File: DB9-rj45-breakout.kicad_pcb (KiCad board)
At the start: 2 copper layers, 32 x 33 mm, 6 parts, among them CN1 1x9, CN2 1x8, SW1 spdt

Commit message: fixed switch to choose 2nd button between up and 2nd button
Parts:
- turned SW1 to 180 degrees
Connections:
- CN2 pad 2: Net-(CN2-Pad2) -> /up
- CN2 pad 7: /b -> Net-(CN2-Pad7)
- SW1 pad 1: /b -> /up
- SW1 pad 2: /up -> Net-(CN2-Pad7)
- SW1 pad 3: Net-(CN2-Pad2) -> /b
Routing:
- net Net-(CN2-Pad7): track 0.00 -> 16.1 mm
- net /b: track 25.4 -> 12.4 mm
- net Net-(CN2-Pad2): track 11.1 -> 0.00 mm
- net /up: track 10.9 -> 20.0 mm
- net /left: track 21.0 -> 20.5 mm
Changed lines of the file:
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@@
     (thickness 1.6)
     (drawings 7)
-    (tracks 43)
+    (tracks 47)
     (zones 0)
     (modules 6)
@@
   (net 8 /GND)
   (net 9 /b)
-  (net 10 "Net-(CN2-Pad2)")
+  (net 10 "Net-(CN2-Pad7)")
   (net_class Default "This is the default net class."
     (clearance 0.2)
@@
     (add_net /up)
     (add_net "Net-(CN1-Pad5)")
-    (add_net "Net-(CN2-Pad2)")
+    (add_net "Net-(CN2-Pad7)")
   )
   (module connectors:DB9 (layer F.Cu)
@@
       (net 7 /5V))
     (pad 7 thru_hole circle (at -2.54 -2.54) (size 1.5 1.5) (drill 0.89) (layers *.Cu *.Mask)
-      (net 9 /b))
+      (net 10 "Net-(CN2-Pad7)"))
     (pad 6 thru_hole circle (at -1.525 -4.32) (size 1.5 1.5) (drill 0.89) (layers *.Cu *.Mask)
       (net 6 /a))
@@
       (net 3 /down))
     (pad 2 thru_hole circle (at 2.535 -4.32) (size 1.5 1.5) (drill 0.89) (layers *.Cu *.Mask)
-      (net 10 "Net-(CN2-Pad2)"))
+      (net 2 /up))
     (pad 1 thru_hole circle (at 3.55 -2.54) (size 1.5 1.5) (drill 0.89) (layers *.Cu *.Mask)
       (net 8 /GND))
@@
   )
   (module switch:100SP1T1B4M2QE (layer F.Cu)
-    (at 150 110.5)
+    (at 150 110.5 180)
     (fp_text reference SW1 (at 0 0) (layer F.Fab) hide
       (effects (font (size 0.5 0.5) (thickness 0.125)))
@@
     (fp_line (start 6.35 3.43) (end 6.35 -3.43) (layer F.Fab) (width 0.12))
     (fp_line (start -6.35 3.43) (end -6.35 -3.43) (layer F.Fab) (width 0.12))
-    (pad 1 thru_hole circle (at -4.7 0) (size 3 3) (drill 1.85) (layers *.Cu *.Mask)
+    (pad 1 thru_hole circle (at -4.7 0 180) (size 3 3) (drill 1.85) (layers *.Cu *.Mask)
+      (net 2 /up))
+    (pad 2 thru_hole circle (at 0 0 180) (size 3 3) (drill 1.85) (layers *.Cu *.Mask)
+      (net 10 "Net-(CN2-Pad7)"))
+    (pad 3 thru_hole circle (at 4.7 0 180) (size 3 3) (drill 1.85) (layers *.Cu *.Mask)
       (net 9 /b))
-    (pad 2 thru_hole circle (at 0 0) (size 3 3) (drill 1.85) (layers *.Cu *.Mask)
-      (net 2 /up))
-    (pad 3 thru_hole circle (at 4.7 0) (size 3 3) (drill 1.85) (layers *.Cu *.Mask)
-      (net 10 "Net-(CN2-Pad2)"))
     (model ${KICAD_SYMBOL_DIR}/3d/e-switch/100SPxT1B4M2xE.stp
       (offset (xyz 0 0 -24))
@@
   (gr_line (start 166 94) (end 166 122) (layer Edge.Cuts) (width 0.05))
   (gr_line (start 134 94) (end 166 94) (layer Edge.Cuts) (width 0.05))
-  (segment (start 155.54 104.96) (end 155.54 101.92) (width 0.5) (layer F.Cu) (net 2))
-  (segment (start 150 110.5) (end 155.54 104.96) (width 0.5) (layer F.Cu) (net 2))
   (segment (start 157 120.786002) (end 157 106.15) (width 0.5) (layer B.Cu) (net 3))
   (segment (start 154.126001 123.660001) (end 157 120.786002) (width 0.5) (layer B.Cu) (net 3))
@@
   (segment (start 153.619999 102.769999) (end 152.77 101.92) (width 0.5) (layer B.Cu) (net 3))
   (segment (start 151.52 122.46) (end 151.54 122.46) (width 0.5) (layer B.Cu) (net 3))
-  (segment (start 150 104.5) (end 150 101.92) (width 0.5) (layer F.Cu) (net 4))
-  (segment (start 147.5 107) (end 150 104.5) (width 0.5) (layer F.Cu) (net 4))
-  (segment (start 147.5 116.61434) (end 147.5 107) (width 0.5) (layer F.Cu) (net 4))
-  (segment (start 150.505 119.61934) (end 147.5 116.61434) (width 0.5) (layer F.Cu) (net 4))
-  (segment (start 150.505 120.68) (end 150.505 119.61934) (width 0.5) (layer F.Cu) (net 4))
   (segment (start 147.23 101.92) (end 147.23 104.27) (width 0.5) (layer B.Cu) (net 5))
   (segment (start 143.349999 108.150001) (end 143.349999 121.349999) (width 0.5) (layer B.Cu) (net 5))
@@
   (segment (start 146.445 120.68) (end 147.5 119.625) (width 0.5) (layer B.Cu) (net 7))
   (segment (start 145.845 109.955) (end 145.3 110.5) (width 0.5) (layer F.Cu) (net 9))
-  (segment (start 145.845 99.08) (end 145.845 109.955) (width 0.5) (layer F.Cu) (net 9))
-  (segment (start 146.39934 122.46) (end 147.46 122.46) (width 0.5) (layer B.Cu) (net 9))
-  (segment (start 145 121.06066) (end 146.39934 122.46) (width 0.5) (layer B.Cu) (net 9))
-  (segment (start 145 112.92132) (end 145 121.06066) (width 0.5) (layer B.Cu) (net 9))
-  (segment (start 145.3 112.62132) (end 145 112.92132) (width 0.5) (layer B.Cu) (net 9))
-  (segment (start 145.3 110.5) (end 145.3 112.62132) (width 0.5) (layer B.Cu) (net 9))
-  (segment (start 154.7 118.515) (end 154.7 110.5) (width 0.5) (layer B.Cu) (net 10))
-  (segment (start 152.535 120.68) (end 154.7 118.515) (width 0.5) (layer B.Cu) (net 10))
+  (segment (start 154.7 118.515) (end 154.7 110.5) (width 0.5) (layer B.Cu) (net 2))
+  (segment (start 152.535 120.68) (end 154.7 118.515) (width 0.5) (layer B.Cu) (net 2))
+  (segment (start 154.7 106.6) (end 154.7 110.5) (width 0.5) (layer F.Cu) (net 2))
+  (segment (start 155.54 105.76) (end 154.7 106.6) (width 0.5) (layer F.Cu) (net 2))
+  (segment (start 155.54 101.92) (end 155.54 105.76) (width 0.5) (layer F.Cu) (net 2))
+  (segment (start 150 104.5) (end 150 101.92) (width 0.5) (layer F.Cu) (net 4))
+  (segment (start 150 105) (end 150 104.5) (width 0.5) (layer F.Cu) (net 4))
+  (segment (start 152.4 107.4) (end 150 105) (width 0.5) (layer F.Cu) (net 4))
+  (segment (start 152.4 117.6) (end 152.4 107.4) (width 0.5) (layer F.Cu) (net 4))
+  (segment (start 150.505 119.495) (end 152.4 117.6) (width 0.5) (layer F.Cu) (net 4))
+  (segment (start 150.505 120.68) (end 150.505 119.495) (width 0.5) (layer F.Cu) (net 4))
+  (segment (start 145.3 108.37868) (end 145.3 110.5) (width 0.5) (layer F.Cu) (net 9))
+  (segment (start 145.845 107.83368) (end 145.3 108.37868) (width 0.5) (layer F.Cu) (net 9))
+  (segment (start 145.845 99.08) (end 145.845 107.83368) (width 0.5) (layer F.Cu) (net 9))
+  (segment (start 145 118.25) (end 150 113.25) (width 0.5) (layer F.Cu) (net 10))
+  (segment (start 145 121.8) (end 145 118.25) (width 0.5) (layer F.Cu) (net 10))
+  (segment (start 150 113.25) (end 150 110.5) (width 0.5) (layer F.Cu) (net 10))
+  (segment (start 145.66 122.46) (end 145 121.8) (width 0.5) (layer F.Cu) (net 10))
+  (segment (start 147.46 122.46) (end 145.66 122.46) (width 0.5) (layer F.Cu) (net 10))
   (zone (net 8) (net_name /GND) (layer F.Cu) (hatch edge 0.508)
     (connect_pads (clearance 0.508))
     (min_thickness 0.254)
-    (fill yes (arc_segments 32) (thermal_gap 0.2) (thermal_bridge_width 0.508))
+    (fill (arc_segments 32) (thermal_gap 0.2) (thermal_bridge_width 0.508))
     (polygon
       (pts
@@
     (connect_pads (clearance 0.508))
     (min_thickness 0.254)
-    (fill yes (arc_segments 32) (thermal_gap 0.2) (thermal_bridge_width 0.508))
+    (fill (arc_segments 32) (thermal_gap 0.2) (thermal_bridge_width 0.508))
     (polygon
       (pts

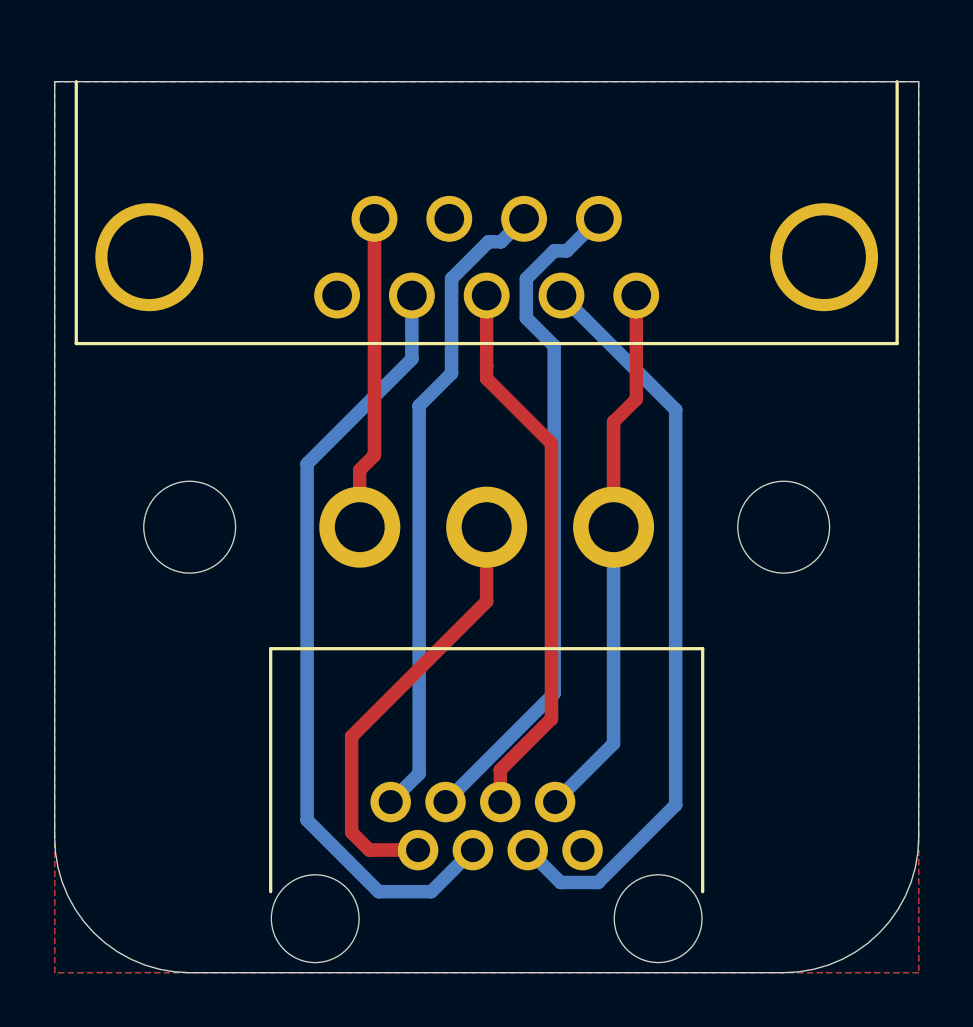
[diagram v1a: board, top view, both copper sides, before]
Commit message: slimmed board down so the DB9 connector can be cut to size
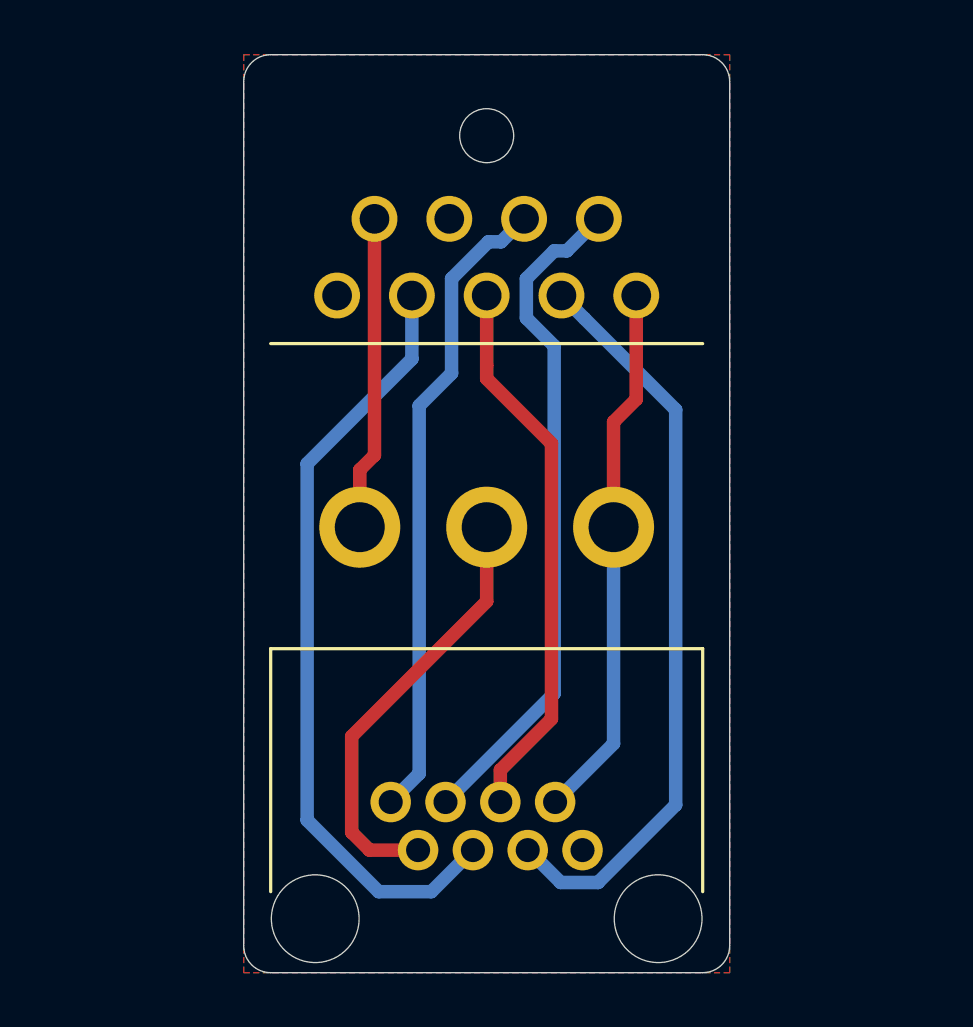
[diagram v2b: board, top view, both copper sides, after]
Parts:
- removed the REF** at (139.0, 110.5)
- removed the REF** at (161.0, 110.5)
- added REF**: M3, PCB:M3, F.Cu at (150.0, 95.0)
- CN1: footprint connectors:DB9 -> connectors:DB9-slim
- moved G*** 8.14 mm to (144.0, 111.0), turned to 270 degrees
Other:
- board size 32 x 33 mm -> 18 x 34 mm
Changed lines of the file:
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@@
   (general
     (thickness 1.6)
-    (drawings 7)
+    (drawings 9)
     (tracks 47)
     (zones 0)
-    (modules 6)
+    (modules 5)
     (nets 11)
   )
@@
     (add_net "Net-(CN2-Pad7)")
   )
-  (module connectors:DB9 (layer F.Cu)
+  (module PCB:M3 (layer F.Cu)
+    (at 150 95)
+    (fp_text reference REF** (at 0 0.5) (layer F.SilkS) hide
+      (effects (font (size 1 1) (thickness 0.15)))
+    )
+    (fp_text value M3 (at 0 -0.5) (layer F.Fab) hide
+      (effects (font (size 1 1) (thickness 0.15)))
+    )
+    (pad "" np_thru_hole circle (at 0 1) (size 2 2) (drill 2) (layers *.Cu *.Mask))
+  )
+  (module connectors:DB9-slim (layer F.Cu)
     (at 150 100 180)
-    (fp_text reference CN1 (at 0 5.5 180) (layer F.Fab)
-      (effects (font (size 1 1) (thickness 0.15)))
-    )
-    (fp_text value 1x9 (at 0 -1 180) (layer F.Fab) hide
-      (effects (font (size 1 1) (thickness 0.15)))
-    )
+    (fp_text reference CN1 (at 0 5.5) (layer F.Fab)
+      (effects (font (size 1 1) (thickness 0.15)))
+    )
+    (fp_text value 1x9 (at 0 -1) (layer F.Fab) hide
+      (effects (font (size 1 1) (thickness 0.15)))
+    )
+    (fp_line (start -8 -3.7) (end 8 -3.7) (layer F.SilkS) (width 0.12))
+    (fp_line (start -15.04 9) (end 15.04 9) (layer F.Fab) (width 0.12))
+    (fp_line (start 15.04 14.8) (end 15.04 -3.5) (layer F.Fab) (width 0.12))
+    (fp_line (start -15.04 14.8) (end -15.04 -3.5) (layer F.Fab) (width 0.12))
+    (fp_line (start -15.04 14.8) (end 15.04 14.8) (layer F.Fab) (width 0.12))
     (fp_line (start -15.04 -3.5) (end 15.04 -3.5) (layer F.Fab) (width 0.12))
-    (fp_line (start -15.04 14.8) (end 15.04 14.8) (layer F.Fab) (width 0.12))
-    (fp_line (start -15.04 14.8) (end -15.04 -3.5) (layer F.Fab) (width 0.12))
-    (fp_line (start 15.04 14.8) (end 15.04 -3.5) (layer F.Fab) (width 0.12))
-    (fp_line (start -15.04 9) (end 15.04 9) (layer F.Fab) (width 0.12))
-    (fp_line (start -15.2 6) (end -15.2 -3.7) (layer F.SilkS) (width 0.12))
-    (fp_line (start -15.2 -3.7) (end 15.2 -3.7) (layer F.SilkS) (width 0.12))
-    (fp_line (start 15.2 -3.7) (end 15.2 6) (layer F.SilkS) (width 0.12))
+    (pad 9 thru_hole circle (at 4.155 0.92 180) (size 1.7 1.7) (drill 1.1) (layers *.Cu *.Mask)
+      (net 9 /b))
+    (pad 8 thru_hole circle (at 1.385 0.92 180) (size 1.7 1.7) (drill 1.1) (layers *.Cu *.Mask)
+      (net 8 /GND))
+    (pad 7 thru_hole circle (at -1.385 0.92 180) (size 1.7 1.7) (drill 1.1) (layers *.Cu *.Mask)
+      (net 7 /5V))
+    (pad 6 thru_hole circle (at -4.155 0.92 180) (size 1.7 1.7) (drill 1.1) (layers *.Cu *.Mask)
+      (net 6 /a))
+    (pad 5 thru_hole circle (at 5.54 -1.92 180) (size 1.7 1.7) (drill 1.1) (layers *.Cu *.Mask)
+      (net 1 "Net-(CN1-Pad5)"))
+    (pad 4 thru_hole circle (at 2.77 -1.92 180) (size 1.7 1.7) (drill 1.1) (layers *.Cu *.Mask)
+      (net 5 /right))
+    (pad 3 thru_hole circle (at 0 -1.92 180) (size 1.7 1.7) (drill 1.1) (layers *.Cu *.Mask)
+      (net 4 /left))
+    (pad 2 thru_hole circle (at -2.77 -1.92 180) (size 1.7 1.7) (drill 1.1) (layers *.Cu *.Mask)
+      (net 3 /down))
     (pad 1 thru_hole circle (at -5.54 -1.92 180) (size 1.7 1.7) (drill 1.1) (layers *.Cu *.Mask)
       (net 2 /up))
-    (pad 2 thru_hole circle (at -2.77 -1.92 180) (size 1.7 1.7) (drill 1.1) (layers *.Cu *.Mask)
-      (net 3 /down))
-    (pad 3 thru_hole circle (at 0 -1.92 180) (size 1.7 1.7) (drill 1.1) (layers *.Cu *.Mask)
-      (net 4 /left))
-    (pad 4 thru_hole circle (at 2.77 -1.92 180) (size 1.7 1.7) (drill 1.1) (layers *.Cu *.Mask)
-      (net 5 /right))
-    (pad 5 thru_hole circle (at 5.54 -1.92 180) (size 1.7 1.7) (drill 1.1) (layers *.Cu *.Mask)
-      (net 1 "Net-(CN1-Pad5)"))
-    (pad 6 thru_hole circle (at -4.155 0.92 180) (size 1.7 1.7) (drill 1.1) (layers *.Cu *.Mask)
-      (net 6 /a))
-    (pad 7 thru_hole circle (at -1.385 0.92 180) (size 1.7 1.7) (drill 1.1) (layers *.Cu *.Mask)
-      (net 7 /5V))
-    (pad 8 thru_hole circle (at 1.385 0.92 180) (size 1.7 1.7) (drill 1.1) (layers *.Cu *.Mask)
-      (net 8 /GND))
-    (pad 9 thru_hole circle (at 4.155 0.92 180) (size 1.7 1.7) (drill 1.1) (layers *.Cu *.Mask)
-      (net 9 /b))
-    (pad 0 thru_hole circle (at 12.495 -0.5 180) (size 4 4) (drill 3.1) (layers *.Cu *.Mask))
-    (pad 0 thru_hole circle (at -12.495 -0.5 180) (size 4 4) (drill 3.1) (layers *.Cu *.Mask))
     (model "${KICAD_SYMBOL_DIR}/3d/DB9 - 203-09SCKKBE.STEP"
       (offset (xyz 0 -9.1 6.5))
@@
   )
   (module logos:gmlogo (layer B.Cu)
-    (at 150 116.5 180)
-    (fp_text reference G*** (at 0 0) (layer B.SilkS) hide
+    (at 144 111 270)
+    (fp_text reference G*** (at 0 0 90) (layer B.SilkS) hide
       (effects (font (size 1.524 1.524) (thickness 0.3)) (justify mirror))
     )
-    (fp_text value LOGO (at 0.75 0) (layer B.SilkS) hide
+    (fp_text value LOGO (at 0.75 0 90) (layer B.SilkS) hide
       (effects (font (size 1.524 1.524) (thickness 0.3)) (justify mirror))
     )
@@
     )
   )
-  (module PCB:M3 (layer F.Cu)
-    (at 139 110.5)
-    (fp_text reference REF** (at 0 0.5) (layer F.SilkS) hide
-      (effects (font (size 1 1) (thickness 0.15)))
-    )
-    (fp_text value M3 (at 0 -0.5) (layer F.Fab) hide
-      (effects (font (size 1 1) (thickness 0.15)))
-    )
-    (pad "" np_thru_hole circle (at 0 0) (size 3.4 3.4) (drill 3.4) (layers *.Cu *.Mask)
-      (solder_mask_margin 1.3))
-  )
-  (module PCB:M3 (layer F.Cu)
-    (at 161 110.5)
-    (fp_text reference REF** (at 0 0.5) (layer F.SilkS) hide
-      (effects (font (size 1 1) (thickness 0.15)))
-    )
-    (fp_text value M3 (at 0 -0.5) (layer F.Fab) hide
-      (effects (font (size 1 1) (thickness 0.15)))
-    )
-    (pad "" np_thru_hole circle (at 0 0) (size 3.4 3.4) (drill 3.4) (layers *.Cu *.Mask)
-      (solder_mask_margin 1.3))
-  )
-  (gr_text "C64 / Amiga" (at 150.5 96.5) (layer B.SilkS)
+  (gr_arc (start 142 94) (end 142 93) (angle -90) (layer Edge.Cuts) (width 0.05))
+  (gr_arc (start 158 94) (end 159 94) (angle -90) (layer Edge.Cuts) (width 0.05))
+  (gr_text "C64 / Amiga" (at 157 113 90) (layer B.SilkS)
     (effects (font (size 2 2) (thickness 0.5)) (justify mirror))
   )
-  (gr_arc (start 139 122) (end 134 122) (angle -90) (layer Edge.Cuts) (width 0.05))
-  (gr_arc (start 161 122) (end 161 127) (angle -90) (layer Edge.Cuts) (width 0.05))
-  (gr_line (start 134 122) (end 134 94) (layer Edge.Cuts) (width 0.05))
-  (gr_line (start 161 127) (end 139 127) (layer Edge.Cuts) (width 0.05))
-  (gr_line (start 166 94) (end 166 122) (layer Edge.Cuts) (width 0.05))
-  (gr_line (start 134 94) (end 166 94) (layer Edge.Cuts) (width 0.05))
+  (gr_arc (start 142 126) (end 141 126) (angle -90) (layer Edge.Cuts) (width 0.05))
+  (gr_arc (start 158 126) (end 158 127) (angle -90) (layer Edge.Cuts) (width 0.05))
+  (gr_line (start 141 126) (end 141 94) (layer Edge.Cuts) (width 0.05))
+  (gr_line (start 158 127) (end 142 127) (layer Edge.Cuts) (width 0.05))
+  (gr_line (start 159 94) (end 159 126) (layer Edge.Cuts) (width 0.05))
+  (gr_line (start 142 93) (end 158 93) (layer Edge.Cuts) (width 0.05))
   (segment (start 157 120.786002) (end 157 106.15) (width 0.5) (layer B.Cu) (net 3))
   (segment (start 154.126001 123.660001) (end 157 120.786002) (width 0.5) (layer B.Cu) (net 3))
@@
     (polygon
       (pts
-        (xy 166 127) (xy 134 127) (xy 134 94) (xy 166 94)
+        (xy 159 127) (xy 141 127) (xy 141 93) (xy 159 93)
       )
     )
@@
     (polygon
       (pts
-        (xy 166 127) (xy 134 127) (xy 134 94) (xy 166 94)
+        (xy 159 127) (xy 141 127) (xy 141 93) (xy 159 93)
       )
     )

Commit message: changed DB9 pinout to female
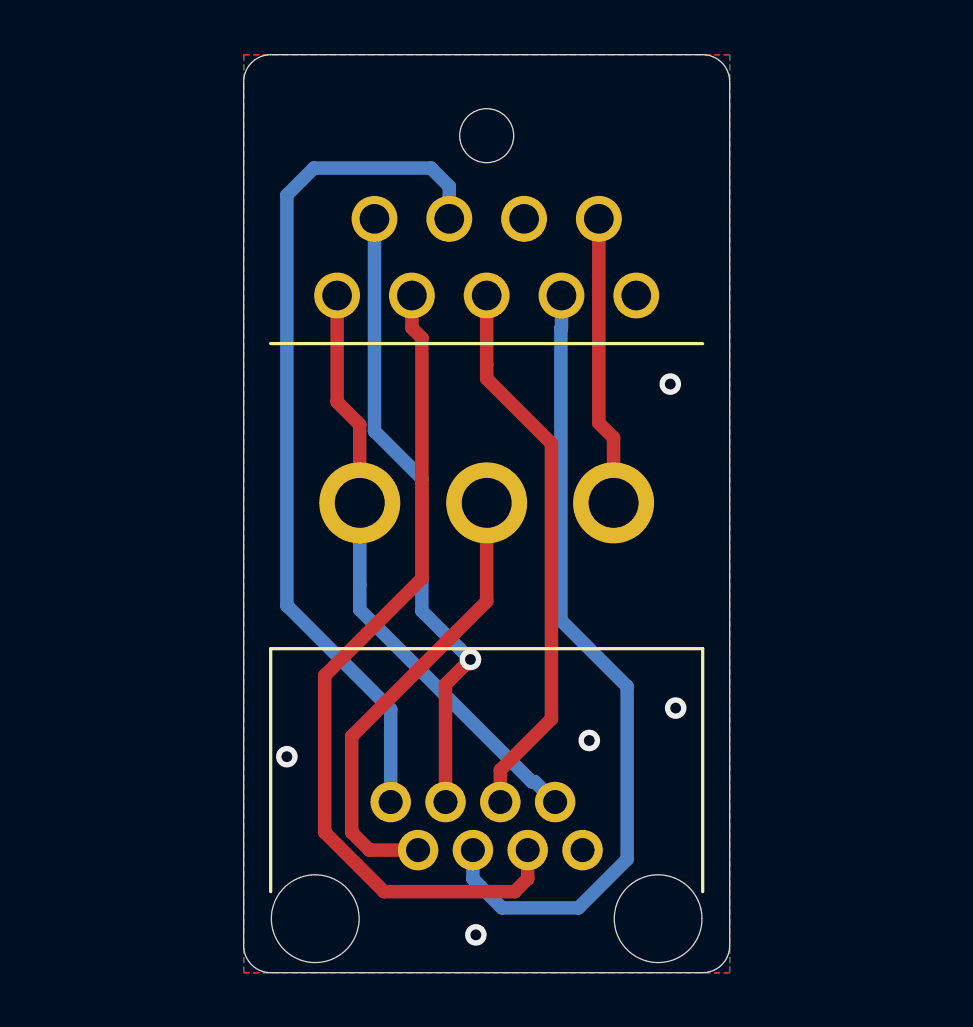
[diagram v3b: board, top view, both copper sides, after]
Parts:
- CN1: footprint connectors:DB9-slim -> connectors:DB9-slim-female
- moved SW1 0.90 mm to (150.0, 109.6), turned to 0 degrees
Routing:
- net /5V: track 23.9 -> 32.0 mm
- net /down: track 27.8 -> 31.2 mm
- net /up: track 20.0 -> 22.2 mm
- net /a: track 25.1 -> 23.5 mm, vias 0 -> 1
- net /right: track 28.9 -> 29.9 mm
- net /b: track 12.4 -> 11.6 mm
- net /GND: vias 0 -> 5
